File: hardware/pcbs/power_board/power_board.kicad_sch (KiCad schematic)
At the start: 3 parts

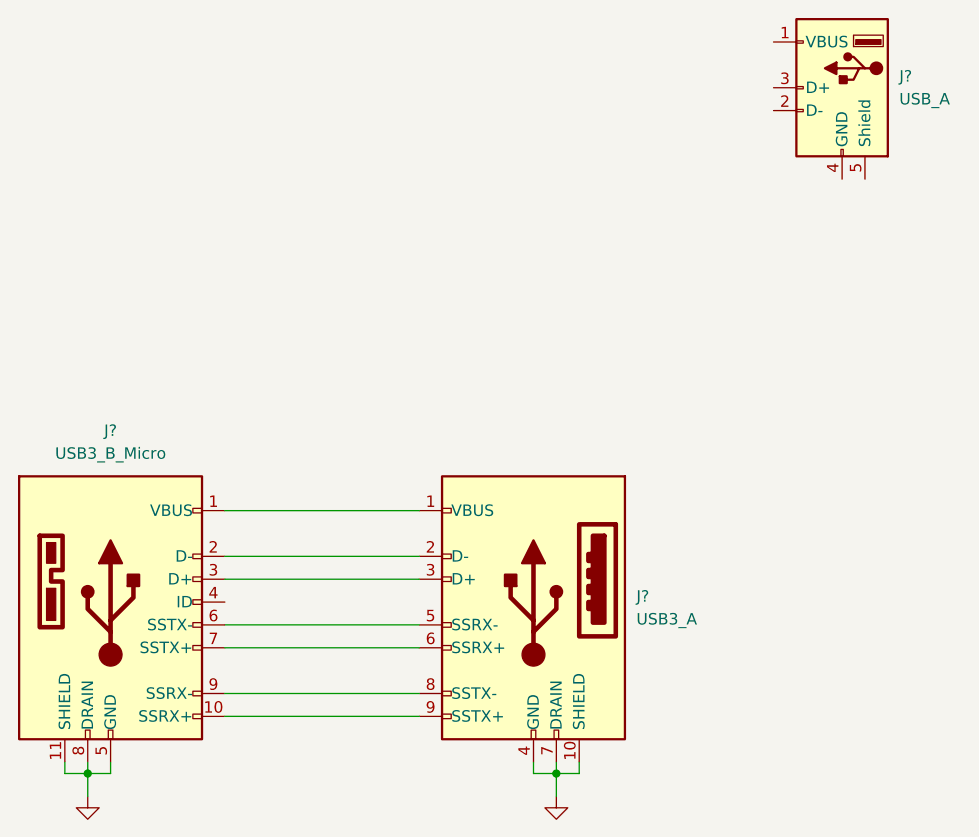
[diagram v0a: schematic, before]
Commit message: power_board: schematic for isolated chargers is done
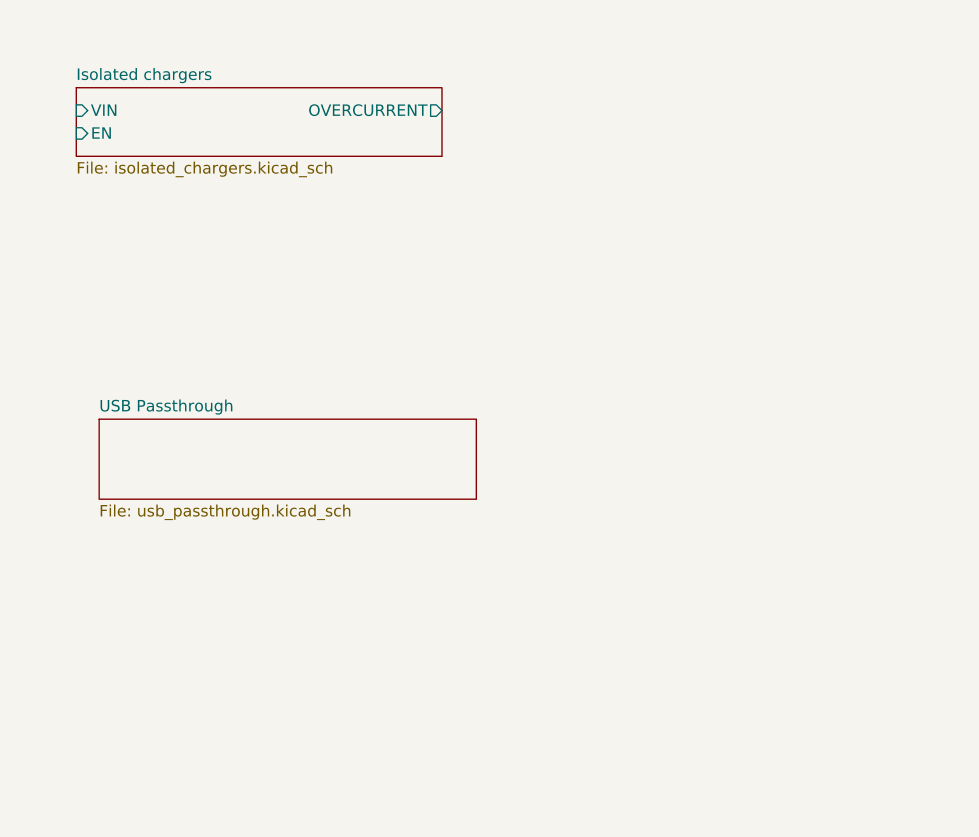
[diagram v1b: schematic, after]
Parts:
- removed J?: USB3_B_Micro, symbol Connector:USB3_B_Micro
- removed J?: USB_A, symbol Connector:USB_A
- removed J?: USB3_A, symbol Connector:USB3_A
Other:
- added sheet Isolated chargers (isolated_chargers.kicad_sch)
- added sheet USB Passthrough (usb_passthrough.kicad_sch)
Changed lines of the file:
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@@
 (kicad_sch (version 20230121) (generator eeschema)
   (paper "A4")
-  (junction (at 166.37 120.65) (diameter 0) (color 0 0 0 0)
-  )
-  (junction (at 114.3 120.65) (diameter 0) (color 0 0 0 0)
-  )
-  (wire (pts (xy 163.83 119.38) (xy 163.83 120.65))
-    (stroke (width 0) (type default))
-  )
-  (wire (pts (xy 129.54 111.76) (xy 151.13 111.76))
-    (stroke (width 0) (type default))
-  )
-  (wire (pts (xy 114.3 120.65) (xy 116.84 120.65))
-    (stroke (width 0) (type default))
-  )
-  (wire (pts (xy 166.37 120.65) (xy 166.37 123.19))
-    (stroke (width 0) (type default))
-  )
-  (wire (pts (xy 129.54 106.68) (xy 151.13 106.68))
-    (stroke (width 0) (type default))
-  )
-  (wire (pts (xy 129.54 91.44) (xy 151.13 91.44))
-    (stroke (width 0) (type default))
-  )
-  (wire (pts (xy 166.37 120.65) (xy 168.91 120.65))
-    (stroke (width 0) (type default))
-  )
-  (wire (pts (xy 114.3 119.38) (xy 114.3 120.65))
-    (stroke (width 0) (type default))
-  )
-  (wire (pts (xy 129.54 99.06) (xy 151.13 99.06))
-    (stroke (width 0) (type default))
-  )
-  (wire (pts (xy 116.84 120.65) (xy 116.84 119.38))
-    (stroke (width 0) (type default))
-  )
-  (wire (pts (xy 166.37 119.38) (xy 166.37 120.65))
-    (stroke (width 0) (type default))
-  )
-  (wire (pts (xy 111.76 120.65) (xy 114.3 120.65))
-    (stroke (width 0) (type default))
-  )
-  (wire (pts (xy 111.76 119.38) (xy 111.76 120.65))
-    (stroke (width 0) (type default))
-  )
-  (wire (pts (xy 129.54 104.14) (xy 151.13 104.14))
-    (stroke (width 0) (type default))
-  )
-  (wire (pts (xy 129.54 114.3) (xy 151.13 114.3))
-    (stroke (width 0) (type default))
-  )
-  (wire (pts (xy 114.3 120.65) (xy 114.3 123.19))
-    (stroke (width 0) (type default))
-  )
-  (wire (pts (xy 129.54 96.52) (xy 151.13 96.52))
-    (stroke (width 0) (type default))
-  )
-  (wire (pts (xy 168.91 120.65) (xy 168.91 119.38))
-    (stroke (width 0) (type default))
-  )
-  (wire (pts (xy 163.83 120.65) (xy 166.37 120.65))
-    (stroke (width 0) (type default))
-  )
-  (symbol (lib_id "Connector:USB3_B_Micro") (at 116.84 101.6 0) (unit 1)
-    (in_bom yes) (on_board yes) (dnp no) (fields_autoplaced)
-    (property "Reference" "J?" (at 116.84 82.55 0)
-      (effects (font (size 1.27 1.27)))
+  (sheet (at 113.03 44.45) (size 40.64 7.62) (fields_autoplaced)
+    (stroke (width 0.1524) (type solid))
+    (fill (color 0 0 0 0.0000))
+    (property "Sheetname" "Isolated chargers" (at 113.03 43.7384 0)
+      (effects (font (size 1.27 1.27)) (justify left bottom))
     )
-    (property "Value" "USB3_B_Micro" (at 116.84 85.09 0)
-      (effects (font (size 1.27 1.27)))
+    (property "Sheetfile" "isolated_chargers.kicad_sch" (at 113.03 52.6546 0)
+      (effects (font (size 1.27 1.27)) (justify left top))
     )
-    (property "Footprint" "" (at 120.65 97.79 0)
-      (effects (font (size 1.27 1.27)) hide)
+    (pin "OVERCURRENT" output (at 153.67 46.99 0)
+      (effects (font (size 1.27 1.27)) (justify right))
     )
-    (property "Datasheet" "~" (at 120.65 96.52 0)
-      (effects (font (size 1.27 1.27)) hide)
+    (pin "VIN" input (at 113.03 46.99 180)
+      (effects (font (size 1.27 1.27)) (justify left))
     )
-    (property "Shop" "https://eu.mouser.com/ProductDetail/Amphenol-Commercial-Products/GSB343K33AHR?qs=8nwx9VzGl4ytGKVAGQNj7w%3D%3D" (at 116.84 101.6 0)
-      (effects (font (size 1.27 1.27)) hide)
+    (pin "EN" input (at 113.03 49.53 180)
+      (effects (font (size 1.27 1.27)) (justify left))
     )
-    (pin "4")
-    (pin "8")
-    (pin "3")
-    (pin "1")
-    (pin "9")
-    (pin "7")
-    (pin "2")
-    (pin "11")
-    (pin "10")
-    (pin "6")
-    (pin "5")
     (instances
       (project "power_board"
-        (path "/4b166175-80a4-48c6-994d-6e62a6160b87"
-          (reference "J?") (unit 1)
-        )
+        (path "/4b166175-80a4-48c6-994d-6e62a6160b87" (page "7"))
       )
     )
   )
-  (symbol (lib_id "power:GND") (at 166.37 123.19 0) (unit 1)
-    (in_bom yes) (on_board yes) (dnp no) (fields_autoplaced)
-    (property "Reference" "#PWR02" (at 166.37 129.54 0)
-      (effects (font (size 1.27 1.27)) hide)
+  (sheet (at 115.57 81.28) (size 41.91 8.89) (fields_autoplaced)
+    (stroke (width 0.1524) (type solid))
+    (fill (color 0 0 0 0.0000))
+    (property "Sheetname" "USB Passthrough" (at 115.57 80.5684 0)
+      (effects (font (size 1.27 1.27)) (justify left bottom))
     )
-    (property "Value" "GND" (at 166.37 128.27 0)
-      (effects (font (size 1.27 1.27)) hide)
+    (property "Sheetfile" "usb_passthrough.kicad_sch" (at 115.57 90.7546 0)
+      (effects (font (size 1.27 1.27)) (justify left top))
     )
-    (property "Footprint" "" (at 166.37 123.19 0)
-      (effects (font (size 1.27 1.27)) hide)
-    )
-    (property "Datasheet" "" (at 166.37 123.19 0)
-      (effects (font (size 1.27 1.27)) hide)
-    )
-    (pin "1")
     (instances
       (project "power_board"
-        (path "/4b166175-80a4-48c6-994d-6e62a6160b87"
-          (reference "#PWR02") (unit 1)
-        )
+        (path "/4b166175-80a4-48c6-994d-6e62a6160b87" (page "2"))
       )
     )
-  )
-  (symbol (lib_id "Connector:USB_A") (at 198.12 44.45 0) (mirror y) (unit 1)
-    (in_bom yes) (on_board yes) (dnp no) (fields_autoplaced)
-    (property "Reference" "J?" (at 204.47 43.18 0)
-      (effects (font (size 1.27 1.27)) (justify right))
-    )
-    (property "Value" "USB_A" (at 204.47 45.72 0)
-      (effects (font (size 1.27 1.27)) (justify right))
-    )
-    (property "Footprint" "" (at 194.31 45.72 0)
-      (effects (font (size 1.27 1.27)) hide)
-    )
-    (property "Datasheet" " ~" (at 194.31 45.72 0)
-      (effects (font (size 1.27 1.27)) hide)
-    )
-    (property "Shop" "https://eu.mouser.com/ProductDetail/Amphenol-Commercial-Products/UE27AC5410H?qs=JOekRM69xWp%2FpXBIdMB8qQ%3D%3D" (at 198.12 44.45 0)
-      (effects (font (size 1.27 1.27)) hide)
-    )
-    (pin "1")
-    (pin "4")
-    (pin "3")
-    (pin "5")
-    (pin "2")
-    (instances
-      (project "power_board"
-        (path "/4b166175-80a4-48c6-994d-6e62a6160b87"
-          (reference "J?") (unit 1)
-        )
-      )
-    )
-  )
-  (symbol (lib_id "power:GND") (at 114.3 123.19 0) (unit 1)
-    (in_bom yes) (on_board yes) (dnp no) (fields_autoplaced)
-    (property "Reference" "#PWR01" (at 114.3 129.54 0)
-      (effects (font (size 1.27 1.27)) hide)
-    )
-    (property "Value" "GND" (at 114.3 128.27 0)
-      (effects (font (size 1.27 1.27)) hide)
-    )
-    (property "Footprint" "" (at 114.3 123.19 0)
-      (effects (font (size 1.27 1.27)) hide)
-    )
-    (property "Datasheet" "" (at 114.3 123.19 0)
-      (effects (font (size 1.27 1.27)) hide)
-    )
-    (pin "1")
-    (instances
-      (project "power_board"
-        (path "/4b166175-80a4-48c6-994d-6e62a6160b87"
-          (reference "#PWR01") (unit 1)
-        )
-      )
-    )
-  )
-  (symbol (lib_id "Connector:USB3_A") (at 163.83 101.6 0) (mirror y) (unit 1)
-    (in_bom yes) (on_board yes) (dnp no) (fields_autoplaced)
-    (property "Reference" "J?" (at 175.26 100.965 0)
-      (effects (font (size 1.27 1.27)) (justify right))
-    )
-    (property "Value" "USB3_A" (at 175.26 103.505 0)
-      (effects (font (size 1.27 1.27)) (justify right))
-    )
-    (property "Footprint" "" (at 160.02 99.06 0)
-      (effects (font (size 1.27 1.27)) hide)
-    )
-    (property "Datasheet" "~" (at 160.02 99.06 0)
-      (effects (font (size 1.27 1.27)) hide)
-    )
-    (property "Shop" "https://eu.mouser.com/ProductDetail/Amphenol-Commercial-Products/GSB3111311HR?qs=f9yNj16SXrLtdMOGrQx7ow%3D%3D" (at 163.83 101.6 0)
-      (effects (font (size 1.27 1.27)) hide)
-    )
-    (pin "9")
-    (pin "1")
-    (pin "10")
-    (pin "8")
-    (pin "6")
-    (pin "5")
-    (pin "4")
-    (pin "3")
-    (pin "2")
-    (pin "7")
-    (instances
-      (project "power_board"
-        (path "/4b166175-80a4-48c6-994d-6e62a6160b87"
-          (reference "J?") (unit 1)
-        )
-      )
-    )

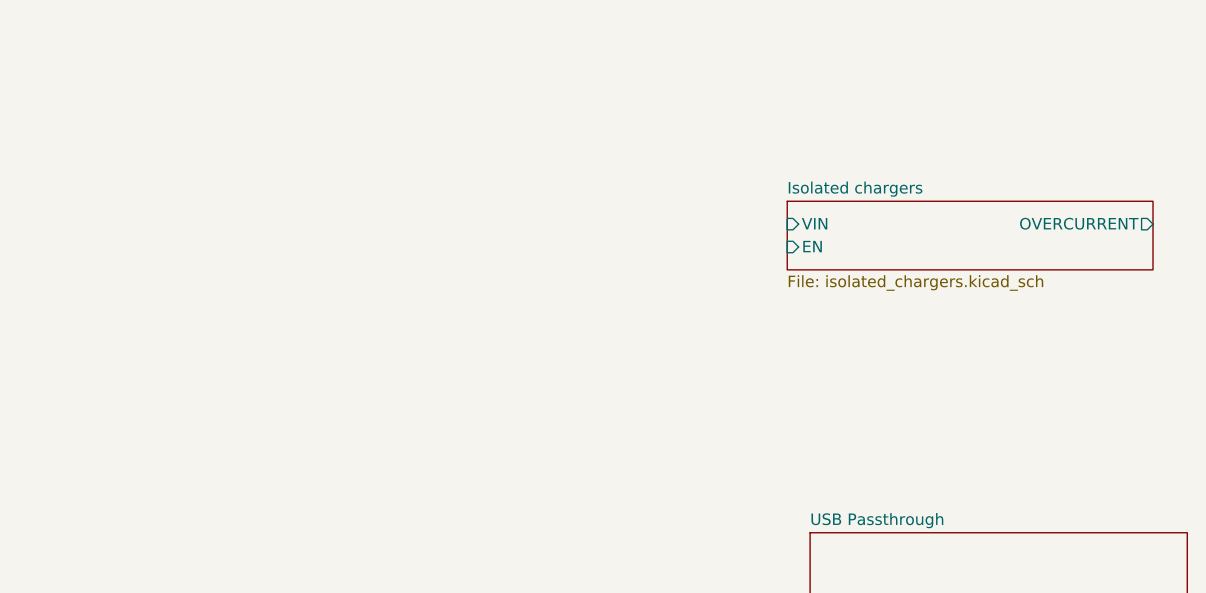
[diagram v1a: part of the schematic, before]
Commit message: power_board: schematic for fan controller
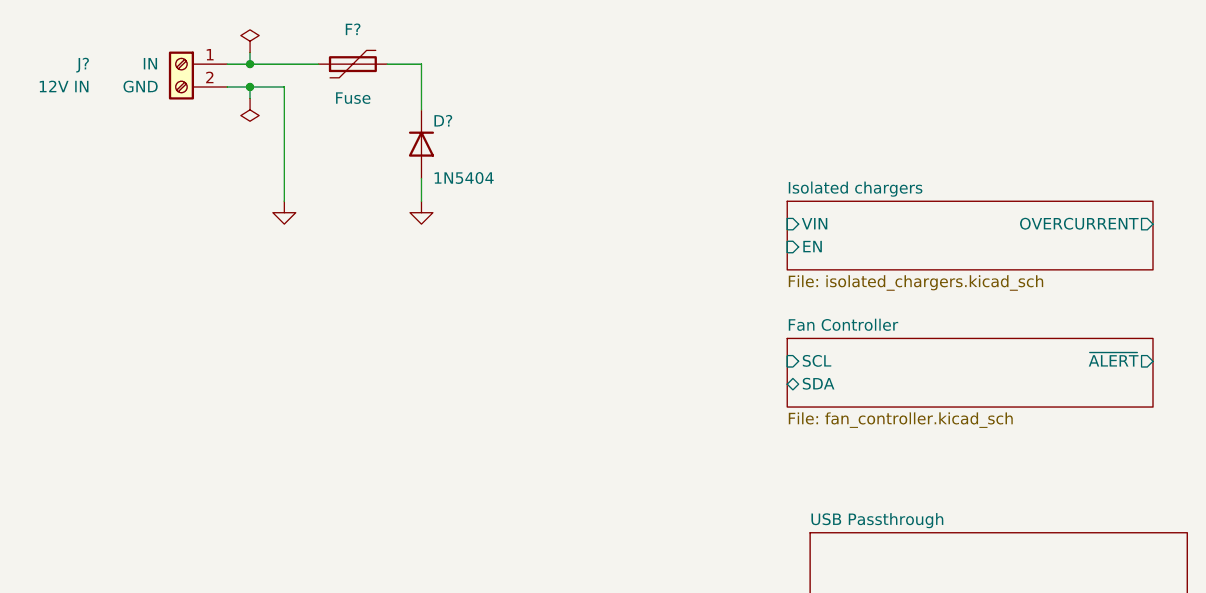
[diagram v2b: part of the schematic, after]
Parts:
- added D?: 1N5404, Diode_THT:D_DO-201AD_P15.24mm_Horizontal, symbol Diode:1N5404
- added F?: Fuse, conn:Fuseholder_Littelfuse_625_series_5x20mm, symbol Device:Polyfuse
- added J?: Screw_Terminal_01x02, conn:TerminalBlock_4Ucon_1x02_P3.50mm_Vertical, symbol conn:Screw_Terminal_01x02
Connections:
- new net: F?.1, J?.1 (Pin_1)
- new net: D?.1 (K), F?.2
- new net GND: D?.2 (A), J?.2 (Pin_2)
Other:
- added sheet Fan Controller (fan_controller.kicad_sch)

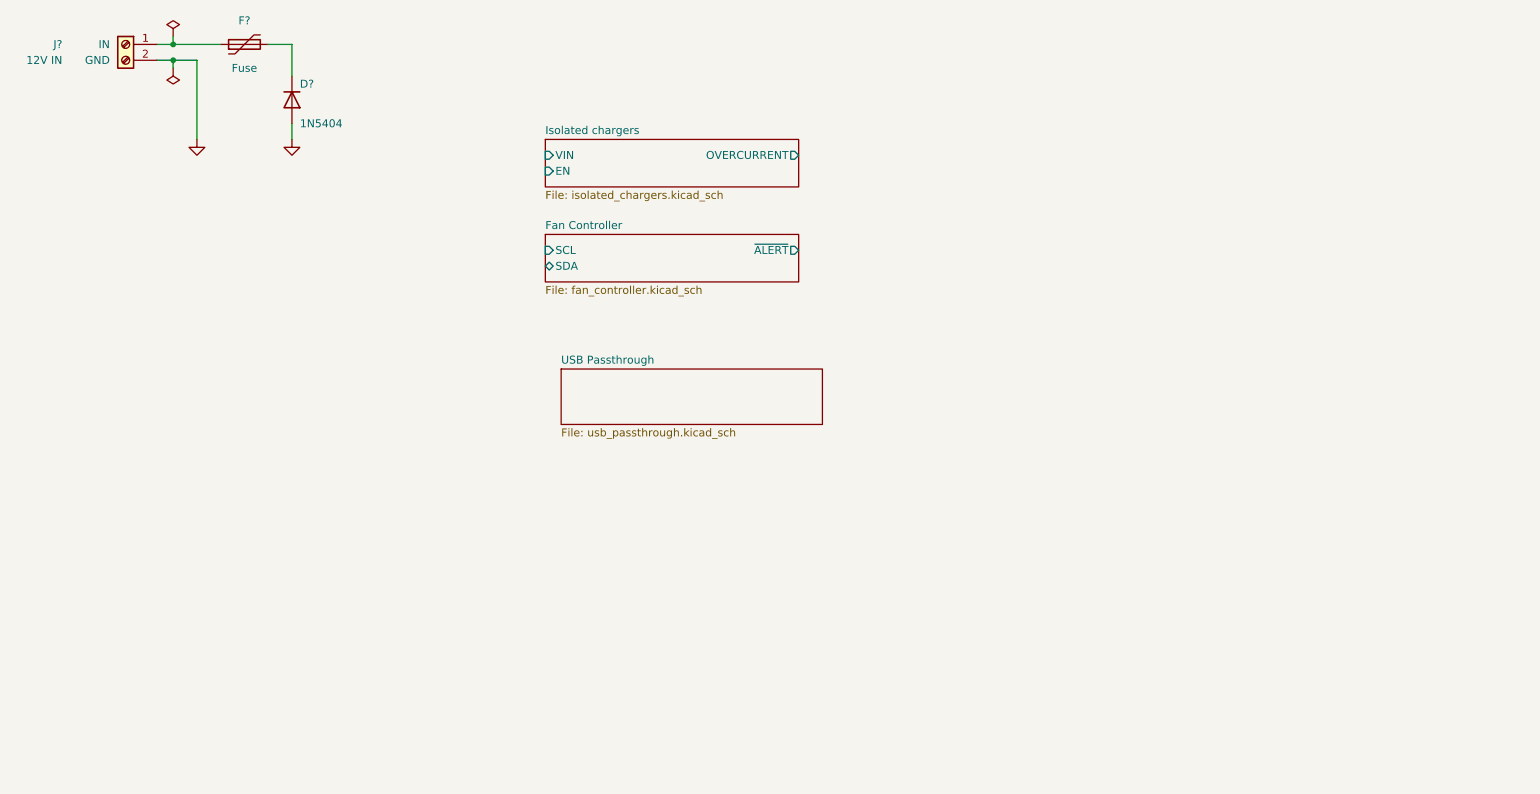
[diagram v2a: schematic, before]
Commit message: power_board: add temperature sensor and GPIOs to schematic
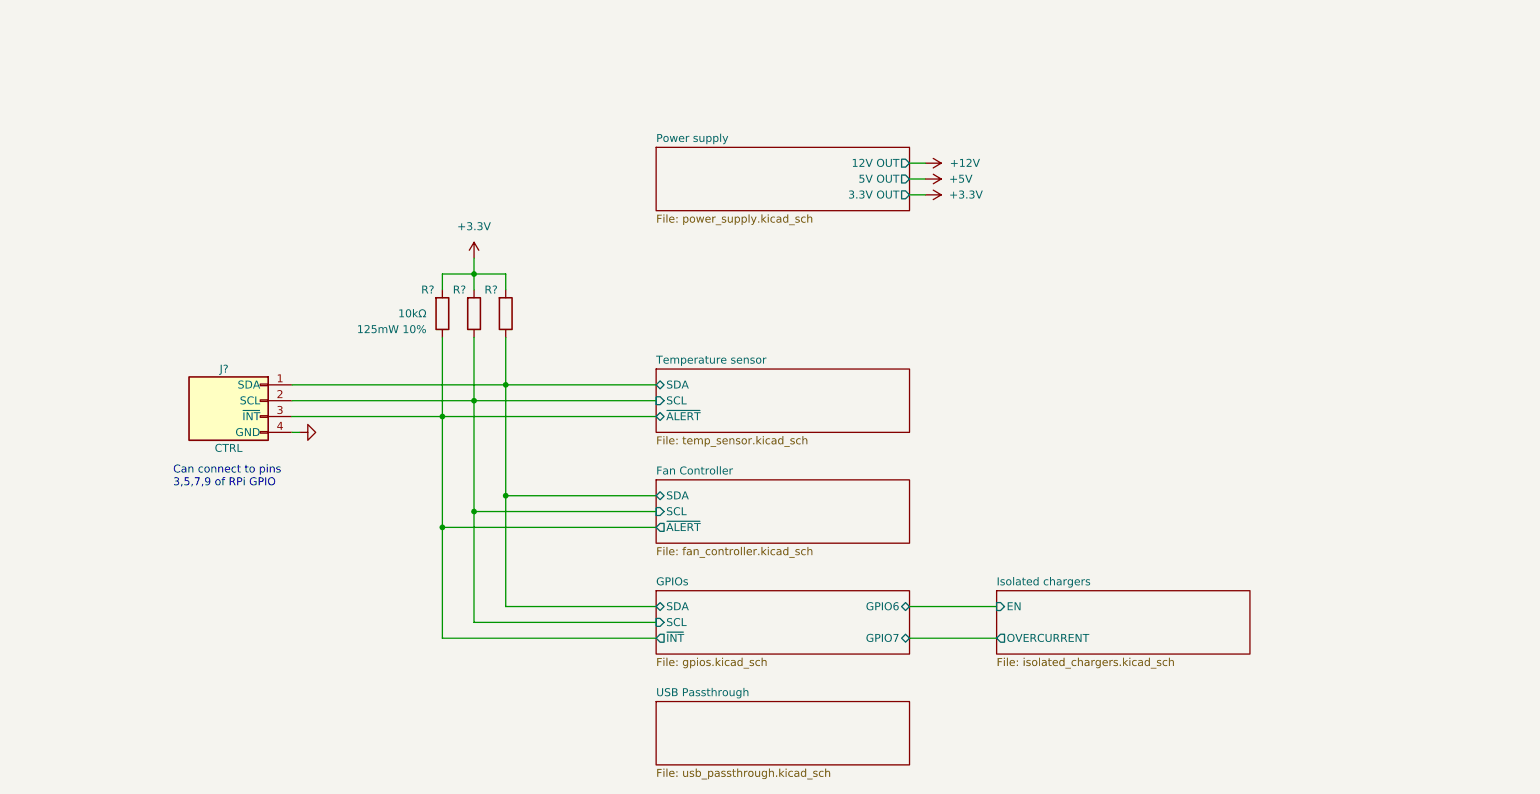
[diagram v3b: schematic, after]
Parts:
- removed D?: 1N5404, Diode_THT:D_DO-201AD_P15.24mm_Horizontal, symbol Diode:1N5404
- removed F?: Fuse, conn:Fuseholder_Littelfuse_625_series_5x20mm, symbol Device:Polyfuse
- removed J?: Screw_Terminal_01x02, conn:TerminalBlock_4Ucon_1x02_P3.50mm_Vertical, symbol conn:Screw_Terminal_01x02
- added J?: Header_01x04, conn:PinHeader_1x04_P2.54mm_Vertical, symbol conn:Conn_01x04
- added R? (x3): 10kΩ, Resistor_SMD:R_0805_2012Metric, symbol Device:R
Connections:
- net Fan Controller/SCL: now also J?.2 (Pin_2), R?.1
- net Fan Controller/SDA: now also J?.1 (Pin_1), R?.1
- net Fan Controller/~{ALERT}: now also J?.3 (Pin_3), R?.1
- net GND: now also J?.4 (Pin_4)
- new net +3.3V: R?.2, R?.2, R?.2
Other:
- added sheet GPIOs (gpios.kicad_sch)
- added sheet Power supply (power_supply.kicad_sch)
- added sheet Temperature sensor (temp_sensor.kicad_sch)
- sheet Isolated chargers ports: added none; removed VIN
- note added: "Can connect to pins 3,5,7,9 of RPi GPIO"
